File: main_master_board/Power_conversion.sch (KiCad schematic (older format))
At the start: 59 parts, among them IC1 IC_MCP73831, U10 FDS4935A, U11 Si1900DL, U12 FDS4935A, U2 LP3852-3.3, U3 TPS61232DRC, U4 LMR16030, U5 Si1900DL, U6 74AUC1G32, U7 INA197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

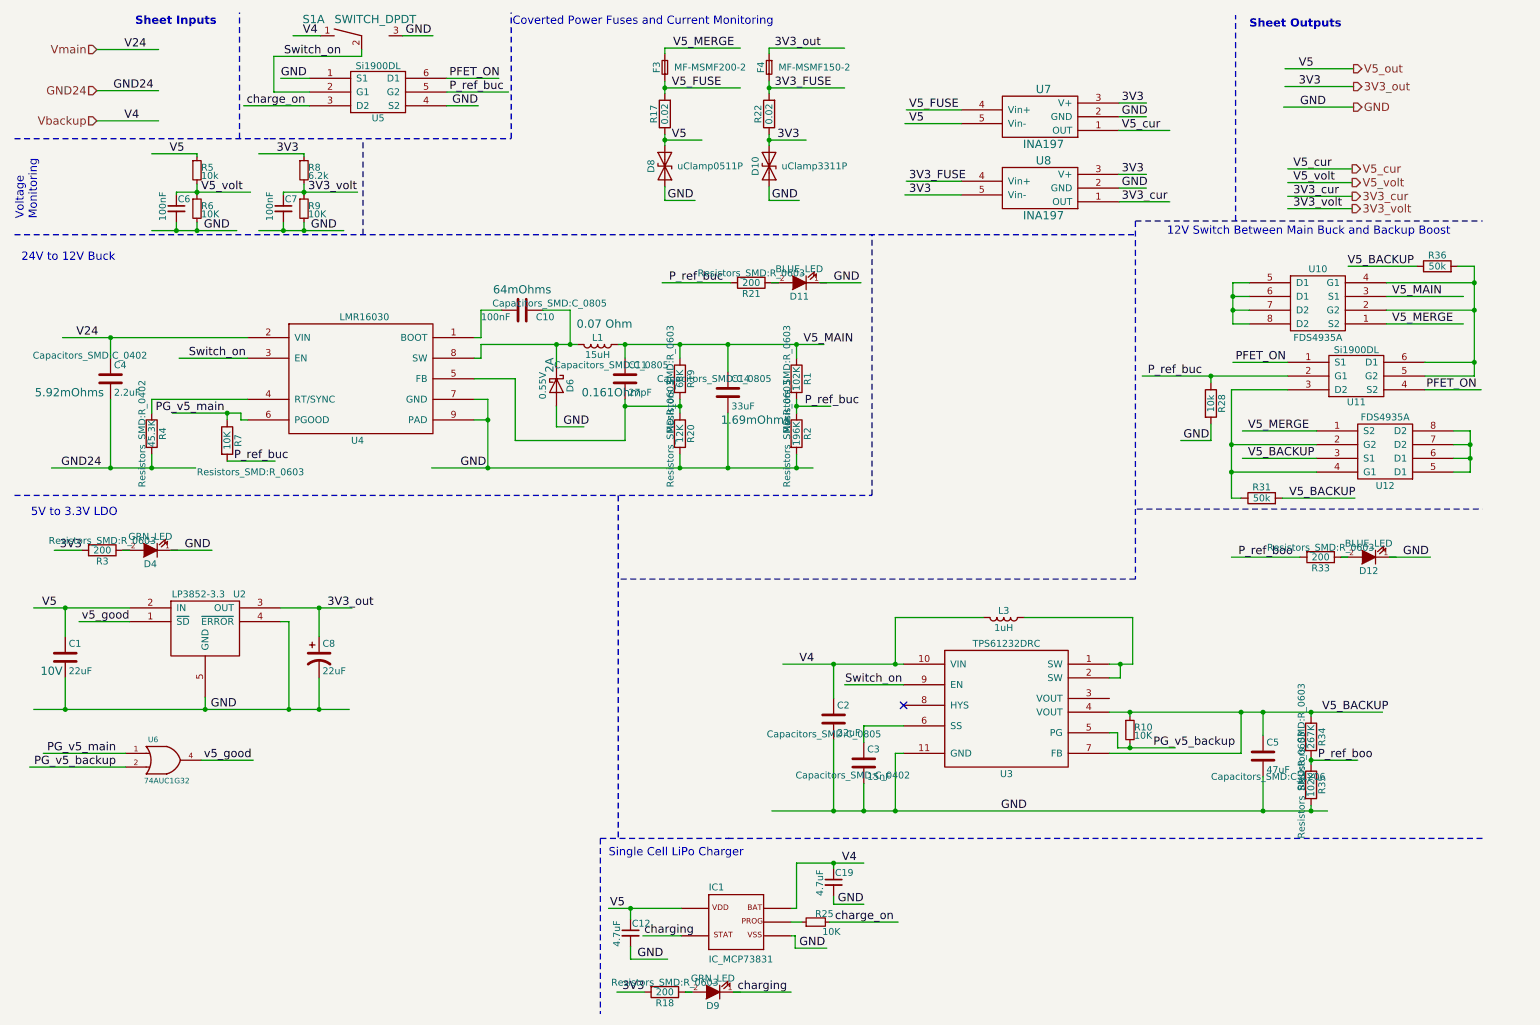
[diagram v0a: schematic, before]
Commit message: Working on moving things to two boards
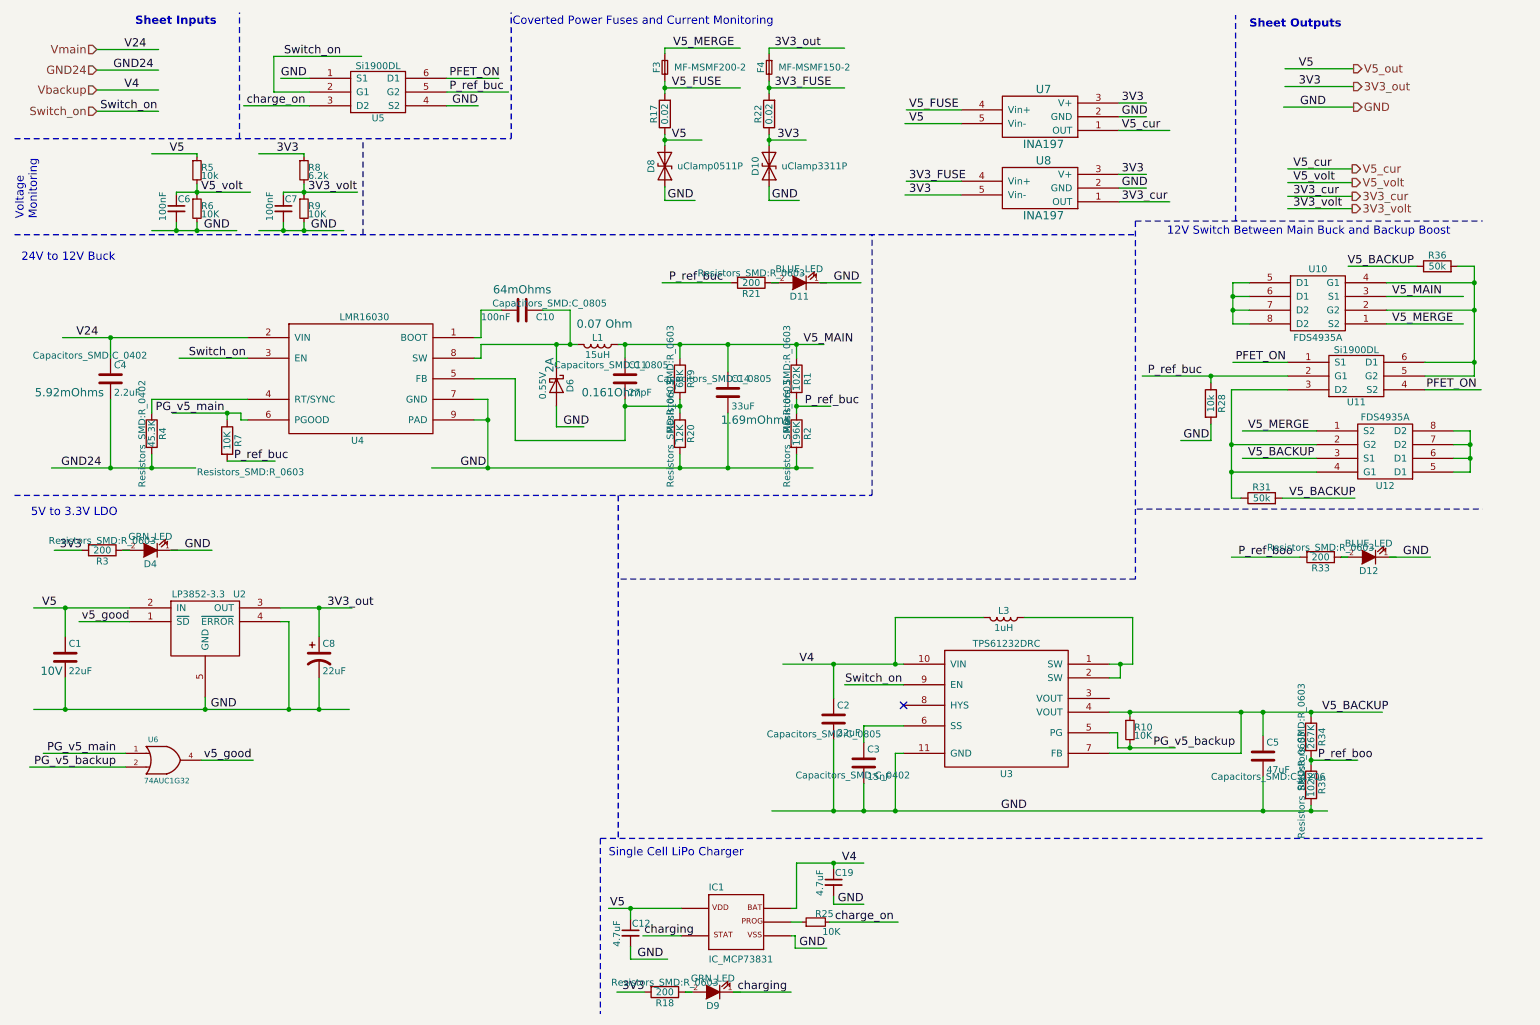
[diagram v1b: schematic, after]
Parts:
- removed S1: SWITCH_DPDT, spdt:SPDT, symbol SWITCH_DPDT
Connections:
- wire segments 213 -> 273

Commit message: Started working on design and layout for fulll board with dart410. Added Macrofab libraries
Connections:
- wire segments 273 -> 211
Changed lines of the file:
@@
 LIBS:Zilog
 LIBS:conn_2x45
+LIBS:MF_Aesthetics
+LIBS:MF_Connectors
+LIBS:MF_Discrete_Semiconductor
+LIBS:MF_Displays
+LIBS:MF_Frequency_Control
+LIBS:MF_IC_Analog
+LIBS:MF_IC_Digital
+LIBS:MF_IC_Power
+LIBS:MF_LEDs
+LIBS:MF_Passives
+LIBS:MF_Sensors
+LIBS:MF_Switches
 LIBS:main_master_board-cache
 EELAYER 25 0
@@
 	2720 4820 2720 5030
 Wire Wire Line
-	2440 4820 2720 4820
-Wire Wire Line
-	2720 4820 2960 4820
+	2440 4820 2960 4820
 Wire Wire Line
 	1100 750  1550 750
@@
 Connection ~ 1500 3800
 Wire Wire Line
-	850  2850 1200 2850
-Wire Wire Line
-	1200 2850 2200 2850
+	850  2850 2200 2850
 Wire Wire Line
 	1200 2850 1200 3000
@@
 	3950 3300 3850 3300
 Wire Wire Line
-	3950 3300 3950 3450
-Wire Wire Line
-	3950 3450 3950 3800
+	3950 3300 3950 3800
 Connection ~ 3950 3800
 Wire Wire Line
@@
 	3900 3000 3900 2900
 Wire Wire Line
-	3900 2900 4450 2900
-Wire Wire Line
-	4450 2900 4550 2900
-Wire Wire Line
-	4550 2900 4600 2900
-Wire Wire Line
-	4900 2900 4950 2900
-Wire Wire Line
-	4950 2900 5350 2900
-Wire Wire Line
-	5350 2900 5700 2900
-Wire Wire Line
-	5700 2900 6200 2900
-Wire Wire Line
-	6200 2900 6400 2900
+	3900 2900 4600 2900
+Wire Wire Line
+	4900 2900 6400 2900
 Wire Wire Line
 	4450 3050 4450 2900
@@
 Connection ~ 5350 3800
 Wire Wire Line
-	5350 3300 5350 3350
-Wire Wire Line
-	5350 3350 5350 3400
-Wire Wire Line
-	4950 3300 4950 3350
-Wire Wire Line
-	4950 3350 4950 3600
+	5350 3300 5350 3400
+Wire Wire Line
+	4950 3300 4950 3600
 Wire Wire Line
 	4950 3600 4150 3600
@@
 	2150 3400 2150 3450
 Wire Wire Line
-	1650 3400 2050 3400
-Wire Wire Line
-	2050 3400 2150 3400
+	1650 3400 2150 3400
 Wire Wire Line
 	2050 3450 2050 3400
@@
 	6200 3350 6450 3350
 Wire Wire Line
-	6200 3300 6200 3350
-Wire Wire Line
-	6200 3350 6200 3400
+	6200 3300 6200 3400
 Wire Wire Line
 	790  4400 990  4400
@@
 	1100 1045 1550 1045
 Wire Wire Line
-	9950 5910 9950 5930
-Wire Wire Line
-	9950 5930 9950 5960
+	9950 5910 9950 5960
 Wire Wire Line
 	9950 5930 10290 5930
@@
 	4770 6500 5710 6500
 Wire Wire Line
-	11110 3530 11110 3630
-Wire Wire Line
-	11110 3630 11110 3730
-Wire Wire Line
-	11110 3730 11110 3830
+	11110 3530 11110 3830
 Wire Wire Line
 	11110 3830 10990 3830
@@
 	9380 2750 9500 2750
 Wire Wire Line
-	9380 2450 9380 2550
-Wire Wire Line
-	9380 2550 9380 2650
-Wire Wire Line
-	9380 2650 9380 2750
+	9380 2450 9380 2750
 Wire Wire Line
 	9380 2450 9500 2450
@@
 	10500 2450 11140 2450
 Wire Wire Line
-	11140 2330 11140 2450
-Wire Wire Line
-	11140 2450 11140 2650
-Wire Wire Line
-	11140 2650 11140 3030
-Wire Wire Line
-	11140 3030 11140 3130
+	11140 2330 11140 3130
 Wire Wire Line
 	11140 2650 10500 2650
@@
 	10500 2750 11060 2750
 Wire Wire Line
-	9370 3230 9370 3630
-Wire Wire Line
-	9370 3630 9370 3830
-Wire Wire Line
-	9370 3830 9370 4020
+	9370 3230 9370 4020
 Wire Wire Line
 	9780 3230 9370 3230
@@
 	9780 3030 9380 3030
 Wire Wire Line
-	8720 3130 9220 3130
-Wire Wire Line
-	9220 3130 9780 3130
+	8720 3130 9780 3130
 Wire Wire Line
 	11140 3130 10780 3130
@@
 	3650 960  4030 960
 Wire Wire Line
-	640  5560 870  5560
-Wire Wire Line
-	870  5560 1890 5560
-Wire Wire Line
-	1890 5560 2500 5560
-Wire Wire Line
-	2500 5560 2720 5560
-Wire Wire Line
-	2720 5560 2940 5560
+	640  5560 2940 5560
 Wire Wire Line
 	1890 5560 1890 5470
@@
 	1340 4920 970  4920
 Wire Wire Line
-	640  4820 870  4820
-Wire Wire Line
-	870  4820 1340 4820
+	640  4820 1340 4820
 Wire Wire Line
 	870  4820 870  5030
@@
 	5240 1030 5790 1030
 Wire Wire Line
-	5240 980  5240 1030
-Wire Wire Line
-	5240 1030 5240 1070
+	5240 980  5240 1070
 Wire Wire Line
 	5240 740  5790 740
@@
 	5240 780  5240 740
 Wire Wire Line
-	5240 1370 5240 1410
-Wire Wire Line
-	5240 1410 5240 1450
+	5240 1370 5240 1450
 Wire Wire Line
 	5240 1410 5510 1410
@@
 	6000 1030 6550 1030
 Wire Wire Line
-	6000 980  6000 1030
-Wire Wire Line
-	6000 1030 6000 1070
+	6000 980  6000 1070
 Wire Wire Line
 	6000 740  6550 740
@@
 	6000 780  6000 740
 Wire Wire Line
-	6000 1370 6000 1410
-Wire Wire Line
-	6000 1410 6000 1450
+	6000 1370 6000 1450
 Wire Wire Line
 	6000 1410 6270 1410
@@
 	2360 1400 4120 1400
 Wire Wire Line
-	1830 1730 1830 1790
-Wire Wire Line
-	1830 1790 1830 1810
-Wire Wire Line
-	1500 2070 1680 2070
-Wire Wire Line
-	1680 2070 1830 2070
-Wire Wire Line
-	1830 2070 2120 2070
+	1830 1730 1830 1810
+Wire Wire Line
+	1500 2070 2120 2070
 Wire Wire Line
 	1680 2010 1680 2070
@@
 	1680 1810 1680 1790
 Wire Wire Line
-	1680 1790 1830 1790
-Wire Wire Line
-	1830 1790 2220 1790
+	1680 1790 2220 1790
 Connection ~ 1830 1790
 Wire Wire Line
-	2610 1730 2610 1790
-Wire Wire Line
-	2610 1790 2610 1810
-Wire Wire Line
-	2280 2070 2460 2070
-Wire Wire Line
-	2460 2070 2610 2070
-Wire Wire Line
-	2610 2070 2900 2070
+	2610 1730 2610 1810
+Wire Wire Line
+	2280 2070 2900 2070
 Wire Wire Line
 	2460 2010 2460 2070
@@
 	2460 1810 2460 1790
 Wire Wire Line
-	2460 1790 2610 1790
-Wire Wire Line
-	2610 1790 3000 1790
+	2460 1790 3000 1790
 Connection ~ 2610 1790
 Wire Notes Line
@@
 	4990 7380 5260 7380
 Wire Wire Line
-	4830 7010 4990 7010
-Wire Wire Line
-	4990 7010 5360 7010
+	4830 7010 5360 7010
 Wire Wire Line
 	4990 7090 4990 7010
@@
 	6200 7010 6200 6680
 Wire Wire Line
-	6200 6680 6470 6680
-Wire Wire Line
-	6470 6680 6690 6680
+	6200 6680 6690 6680
 Wire Wire Line
 	6470 6680 6470 6720
@@
 	8680 4100 11200 4100
 Wire Wire Line
-	770  3800 1200 3800
-Wire Wire Line
-	1200 3800 1500 3800
-Wire Wire Line
-	1500 3800 1820 3800
-Wire Wire Line
-	3540 3800 3950 3800
-Wire Wire Line
-	3950 3800 5350 3800
-Wire Wire Line
-	5350 3800 5700 3800
-Wire Wire Line
-	5700 3800 6200 3800
-Wire Wire Line
-	6200 3800 6320 3800
+	770  3800 1820 3800
+Wire Wire Line
+	3540 3800 6320 3800
 Wire Wire Line
 	6200 3700 6200 3800
@@
 	10260 1170 9750 1170
 Wire Wire Line
-	6020 6300 6470 6300
-Wire Wire Line
-	6470 6300 6690 6300
-Wire Wire Line
-	6690 6300 6920 6300
-Wire Wire Line
-	6920 6300 9600 6300
-Wire Wire Line
-	9600 6300 9950 6300
-Wire Wire Line
-	9950 6300 10070 6300
+	6020 6300 10070 6300
 Wire Wire Line
 	6980 5880 6920 5880
@@
 Connection ~ 6690 6300
 Wire Wire Line
-	6100 5230 6470 5230
-Wire Wire Line
-	6470 5230 6920 5230
-Wire Wire Line
-	6920 5230 6980 5230
+	6100 5230 6980 5230
 Wire Wire Line
 	6470 5230 6470 5480
@@
 Connection ~ 6920 5230
 Wire Wire Line
-	8480 5230 8560 5230
-Wire Wire Line
-	8560 5230 8650 5230
+	8480 5230 8650 5230
 Wire Wire Line
 	8650 5230 8650 4890
@@
 Connection ~ 8560 5230
 Wire Wire Line
-	8480 5580 8630 5580
-Wire Wire Line
-	8630 5580 9440 5580
-Wire Wire Line
-	9440 5580 9600 5580
-Wire Wire Line
-	9600 5580 9950 5580
-Wire Wire Line
-	9950 5580 10470 5580
+	8480 5580 10470 5580
 $Comp
 L R_Small R10
@@
 	8540 5730 8540 5840
 Wire Wire Line
-	8540 5840 8630 5840
-Wire Wire Line
-	8630 5840 8960 5840
+	8540 5840 8960 5840
 Wire Wire Line
 	8630 5840 8630 5810

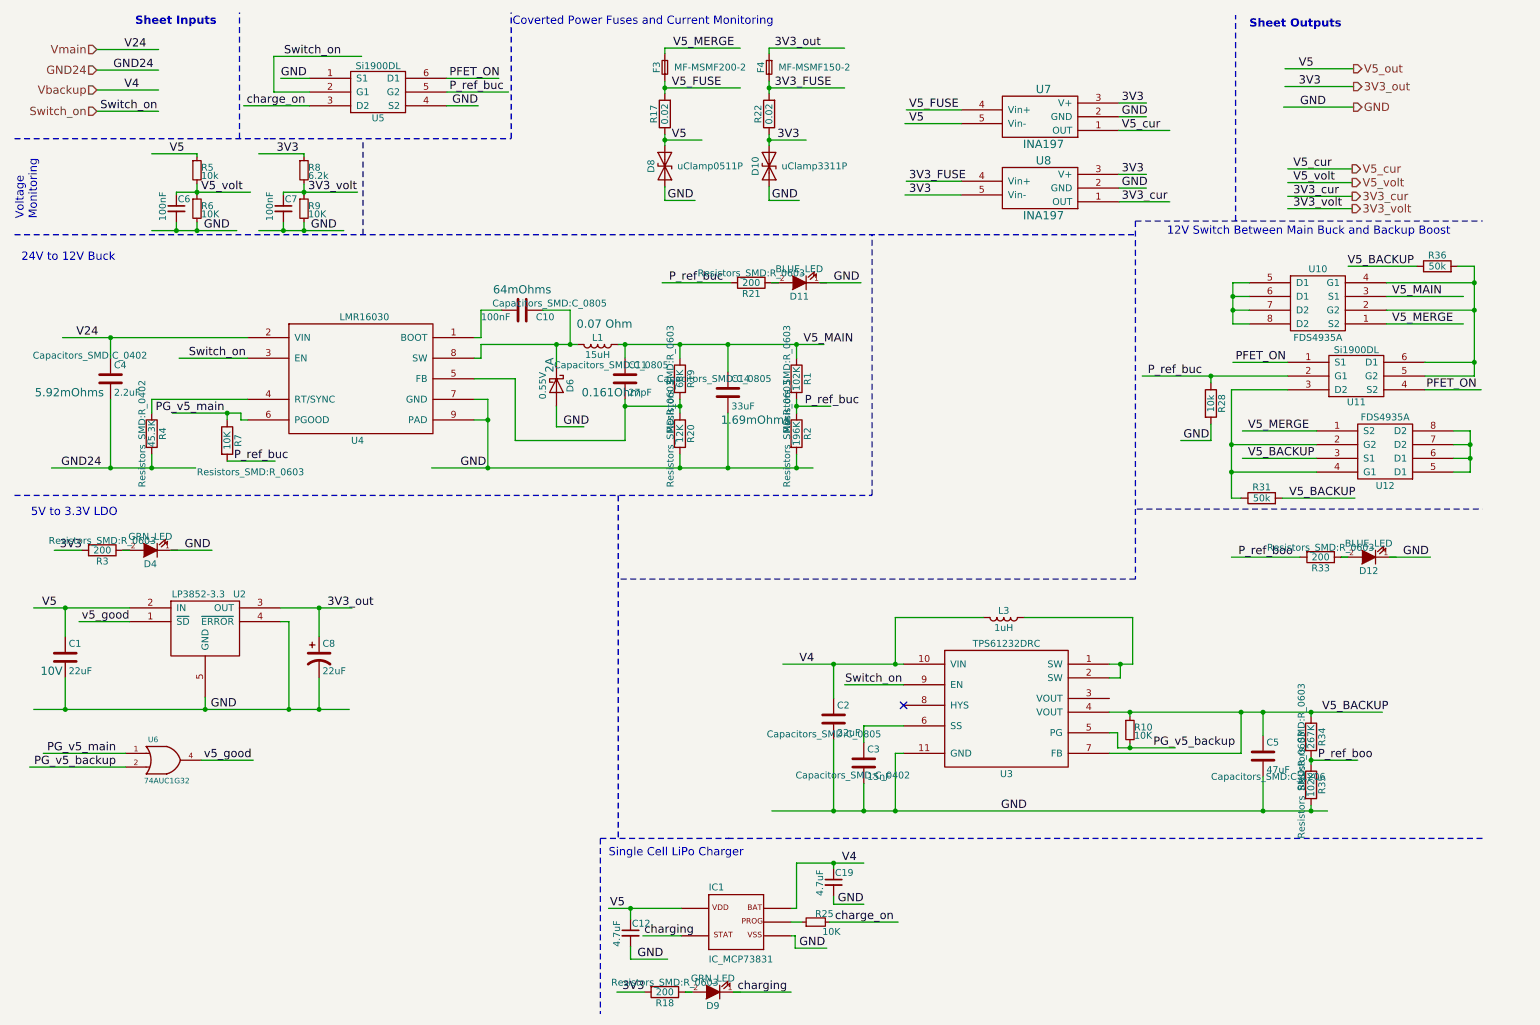
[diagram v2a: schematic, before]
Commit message: Added a lot of things. Put a 5v to 4v buck as well as supporing the snapdragon board
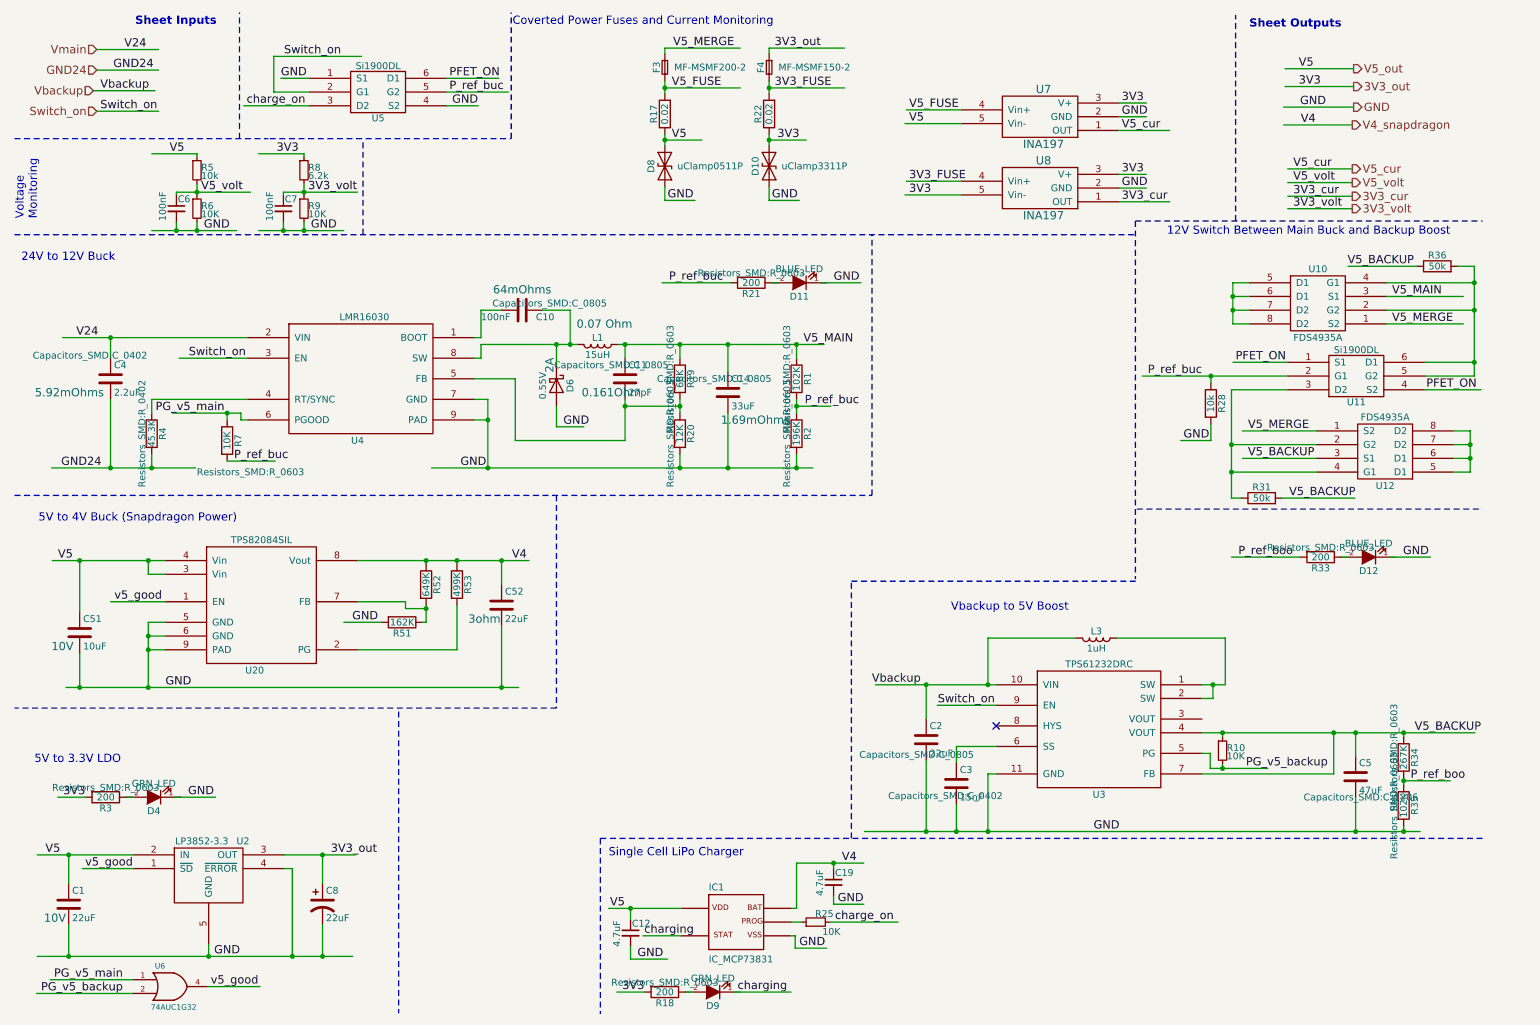
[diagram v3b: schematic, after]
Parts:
- added C51: 10uF, Capacitors_SMD:C_0805, symbol C
- added C52: 22uF, Capacitors_SMD:C_1210, symbol C
- added R51: 162K, Resistors_SMD:R_0402, symbol R
- added R52: 649K, Resistors_SMD:R_0402, symbol R
- added R53: 499K, Resistors_SMD:R_0402, symbol R
- added U20: TPS82084SIL, uSIP-8:uSIP-8, symbol TPS82084SIL
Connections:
- net labels added: V4_snapdragon
- wire segments 211 -> 236
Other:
- note added: "5V to 4V Buck (Snapdragon Power)"
- note added: "Vbackup to 5V Boost"
- moved on the sheet: C1, C2, C3, C5, C8, D4, L3, R10, R3, R34, R35, U2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
